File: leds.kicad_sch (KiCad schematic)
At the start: 10 parts, among them U10 SK9822, U11 SK9822, U12 SK9822, U13 SK9822, U14 SK9822

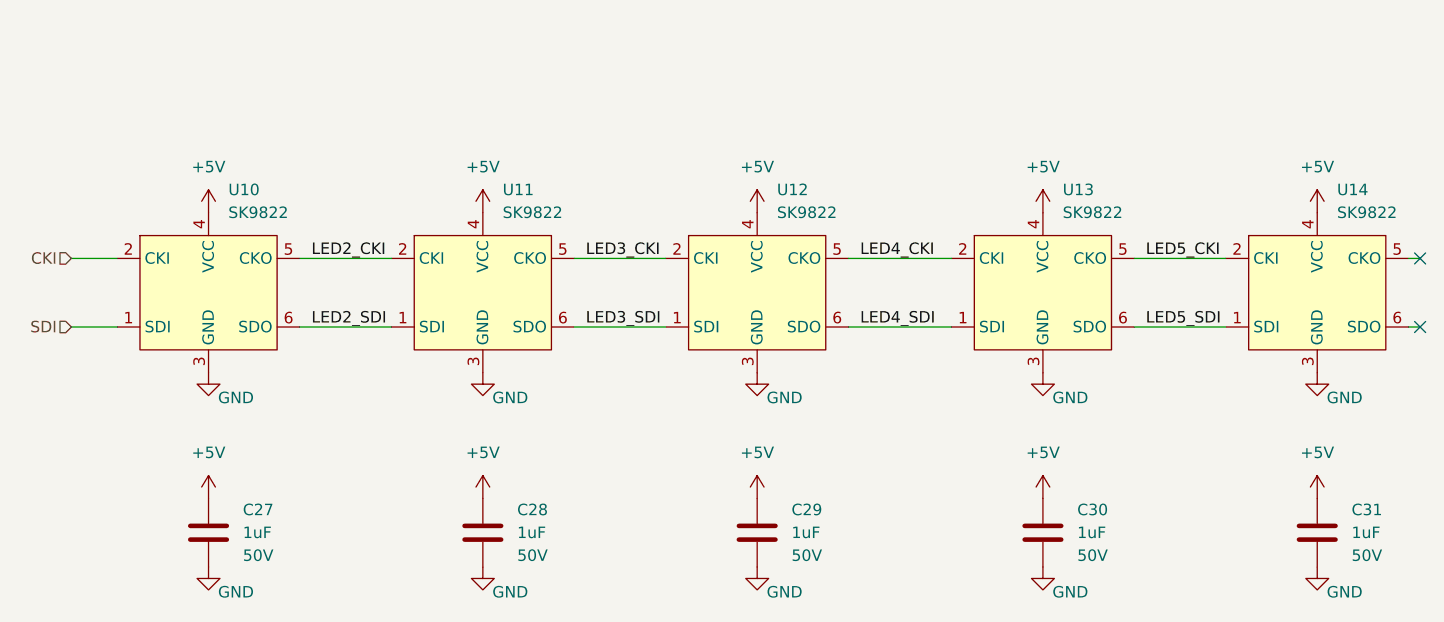
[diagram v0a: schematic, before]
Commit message: Added STM32 MCU with prelim pinout to the schematic
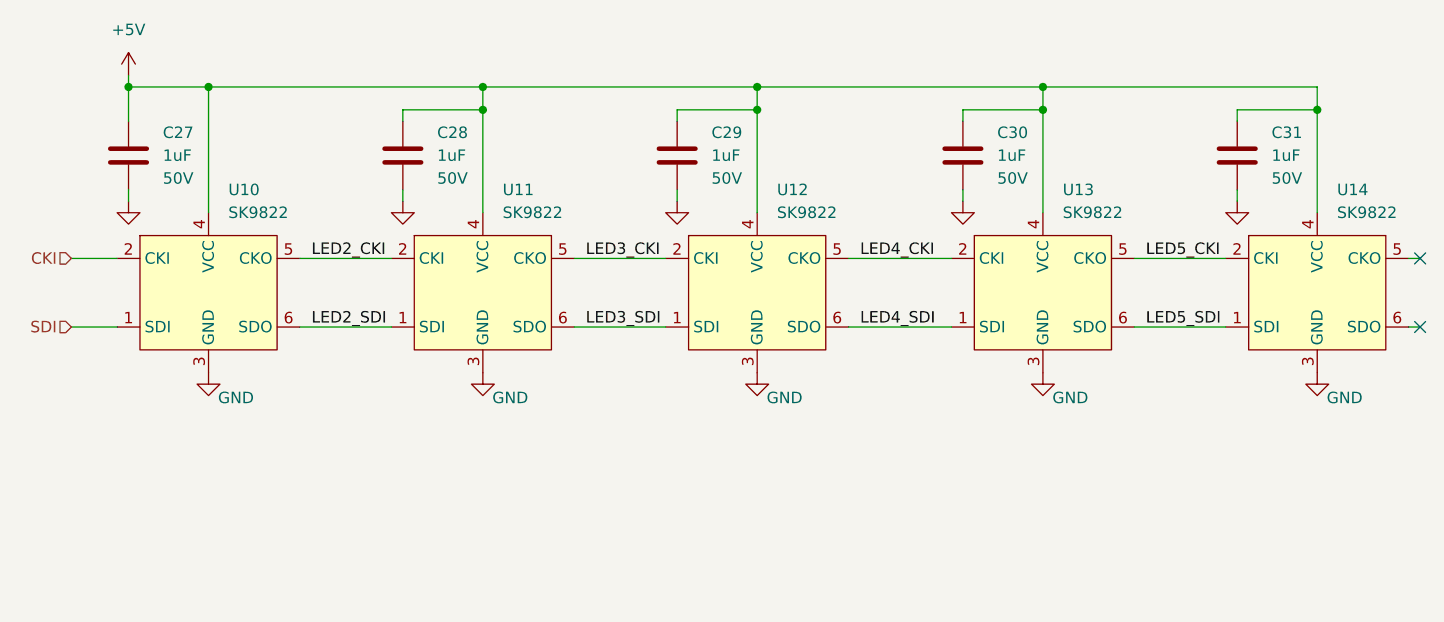
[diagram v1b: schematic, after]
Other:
- moved on the sheet: C27, C28, C29, C30, C31

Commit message: Prelim connector pinout defined.  Re-annotated all parts
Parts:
- renumbered C27 to C17, C28 to C18, C29 to C19, C30 to C20, C31 to C21, U10 to U4, U11 to U5, U12 to U6, U13 to U7, U14 to U8
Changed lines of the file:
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@@
 		(on_board yes)
 		(dnp no)
-		(property "Reference" "#PWR043"
+		(property "Reference" "#PWR0108"
 			(at 194.31 85.09 0)
 			(effects
@@
 			(project "lmc_media_blitz"
 				(path "/b87eb037-3127-4116-a225-5eb939725614/fa7871a6-f26c-496a-b2cd-c50953503e39"
-					(reference "#PWR043")
+					(reference "#PWR0108")
 					(unit 1)
 				)
@@
 		(dnp no)
 		(fields_autoplaced yes)
-		(property "Reference" "U10"
+		(property "Reference" "U4"
 			(at 82.2041 77.47 0)
 			(effects
@@
 			(project "lmc_media_blitz"
 				(path "/b87eb037-3127-4116-a225-5eb939725614/fa7871a6-f26c-496a-b2cd-c50953503e39"
-					(reference "U10")
+					(reference "U4")
 					(unit 1)
 				)
@@
 		(on_board yes)
 		(dnp no)
-		(property "Reference" "#PWR037"
+		(property "Reference" "#PWR0103"
 			(at 101.6 85.09 0)
 			(effects
@@
 			(project "lmc_media_blitz"
 				(path "/b87eb037-3127-4116-a225-5eb939725614/fa7871a6-f26c-496a-b2cd-c50953503e39"
-					(reference "#PWR037")
+					(reference "#PWR0103")
 					(unit 1)
 				)
@@
 		(on_board yes)
 		(dnp no)
-		(property "Reference" "#PWR039"
+		(property "Reference" "#PWR0102"
 			(at 132.08 85.09 0)
 			(effects
@@
 			(project "lmc_media_blitz"
 				(path "/b87eb037-3127-4116-a225-5eb939725614/fa7871a6-f26c-496a-b2cd-c50953503e39"
-					(reference "#PWR039")
+					(reference "#PWR0102")
 					(unit 1)
 				)
@@
 		(dnp no)
 		(fields_autoplaced yes)
-		(property "Reference" "U13"
+		(property "Reference" "U7"
 			(at 174.9141 77.47 0)
 			(effects
@@
 			(project "lmc_media_blitz"
 				(path "/b87eb037-3127-4116-a225-5eb939725614/fa7871a6-f26c-496a-b2cd-c50953503e39"
-					(reference "U13")
+					(reference "U7")
 					(unit 1)
 				)
@@
 		(dnp no)
 		(fields_autoplaced yes)
-		(property "Reference" "C29"
+		(property "Reference" "C19"
 			(at 135.89 71.1199 0)
 			(effects
@@
 			(project "lmc_media_blitz"
 				(path "/b87eb037-3127-4116-a225-5eb939725614/fa7871a6-f26c-496a-b2cd-c50953503e39"
-					(reference "C29")
+					(reference "C19")
 					(unit 1)
 				)
@@
 		(dnp no)
 		(fields_autoplaced yes)
-		(property "Reference" "U12"
+		(property "Reference" "U6"
 			(at 143.1641 77.47 0)
 			(effects
@@
 			(project "lmc_media_blitz"
 				(path "/b87eb037-3127-4116-a225-5eb939725614/fa7871a6-f26c-496a-b2cd-c50953503e39"
-					(reference "U12")
+					(reference "U6")
 					(unit 1)
 				)
@@
 		(on_board yes)
 		(dnp no)
-		(property "Reference" "#PWR053"
+		(property "Reference" "#PWR0105"
 			(at 80.01 104.14 0)
 			(effects
@@
 			(project "lmc_media_blitz"
 				(path "/b87eb037-3127-4116-a225-5eb939725614/fa7871a6-f26c-496a-b2cd-c50953503e39"
-					(reference "#PWR053")
+					(reference "#PWR0105")
 					(unit 1)
 				)
@@
 		(dnp no)
 		(fields_autoplaced yes)
-		(property "Reference" "U14"
+		(property "Reference" "U8"
 			(at 205.3941 77.47 0)
 			(effects
@@
 			(project "lmc_media_blitz"
 				(path "/b87eb037-3127-4116-a225-5eb939725614/fa7871a6-f26c-496a-b2cd-c50953503e39"
-					(reference "U14")
+					(reference "U8")
 					(unit 1)
 				)
@@
 		(on_board yes)
 		(dnp no)
-		(property "Reference" "#PWR034"
+		(property "Reference" "#PWR0104"
 			(at 71.12 85.09 0)
 			(effects
@@
 			(project "lmc_media_blitz"
 				(path "/b87eb037-3127-4116-a225-5eb939725614/fa7871a6-f26c-496a-b2cd-c50953503e39"
-					(reference "#PWR034")
+					(reference "#PWR0104")
 					(unit 1)
 				)
@@
 		(on_board yes)
 		(dnp no)
-		(property "Reference" "#PWR061"
+		(property "Reference" "#PWR0107"
 			(at 203.2 104.14 0)
 			(effects
@@
 			(project "lmc_media_blitz"
 				(path "/b87eb037-3127-4116-a225-5eb939725614/fa7871a6-f26c-496a-b2cd-c50953503e39"
-					(reference "#PWR061")
+					(reference "#PWR0107")
 					(unit 1)
 				)
@@
 		(dnp no)
 		(fields_autoplaced yes)
-		(property "Reference" "U11"
+		(property "Reference" "U5"
 			(at 112.6841 77.47 0)
 			(effects
@@
 			(project "lmc_media_blitz"
 				(path "/b87eb037-3127-4116-a225-5eb939725614/fa7871a6-f26c-496a-b2cd-c50953503e39"
-					(reference "U11")
+					(reference "U5")
 					(unit 1)
 				)
@@
 		(dnp no)
 		(fields_autoplaced yes)
-		(property "Reference" "#PWR052"
+		(property "Reference" "#PWR0101"
 			(at 71.12 68.58 0)
 			(effects
@@
 			(project "lmc_media_blitz"
 				(path "/b87eb037-3127-4116-a225-5eb939725614/fa7871a6-f26c-496a-b2cd-c50953503e39"
-					(reference "#PWR052")
+					(reference "#PWR0101")
 					(unit 1)
 				)
@@
 		(on_board yes)
 		(dnp no)
-		(property "Reference" "#PWR057"
+		(property "Reference" "#PWR0109"
 			(at 140.97 104.14 0)
 			(effects
@@
 			(project "lmc_media_blitz"
 				(path "/b87eb037-3127-4116-a225-5eb939725614/fa7871a6-f26c-496a-b2cd-c50953503e39"
-					(reference "#PWR057")
+					(reference "#PWR0109")
 					(unit 1)
 				)
@@
 		(dnp no)
 		(fields_autoplaced yes)
-		(property "Reference" "C27"
+		(property "Reference" "C17"
 			(at 74.93 71.1199 0)
 			(effects
@@
 			(project "lmc_media_blitz"
 				(path "/b87eb037-3127-4116-a225-5eb939725614/fa7871a6-f26c-496a-b2cd-c50953503e39"
-					(reference "C27")
+					(reference "C17")
 					(unit 1)
 				)
@@
 		(on_board yes)
 		(dnp no)
-		(property "Reference" "#PWR059"
+		(property "Reference" "#PWR0111"
 			(at 172.72 104.14 0)
 			(effects
@@
 			(project "lmc_media_blitz"
 				(path "/b87eb037-3127-4116-a225-5eb939725614/fa7871a6-f26c-496a-b2cd-c50953503e39"
-					(reference "#PWR059")
+					(reference "#PWR0111")
 					(unit 1)
 				)
@@
 		(dnp no)
 		(fields_autoplaced yes)
-		(property "Reference" "C31"
+		(property "Reference" "C21"
 			(at 198.12 71.1199 0)
 			(effects
@@
 			(project "lmc_media_blitz"
 				(path "/b87eb037-3127-4116-a225-5eb939725614/fa7871a6-f26c-496a-b2cd-c50953503e39"
-					(reference "C31")
+					(reference "C21")
 					(unit 1)
 				)
@@
 		(dnp no)
 		(fields_autoplaced yes)
-		(property "Reference" "C28"
+		(property "Reference" "C18"
 			(at 105.41 71.1199 0)
 			(effects
@@
 			(project "lmc_media_blitz"
 				(path "/b87eb037-3127-4116-a225-5eb939725614/fa7871a6-f26c-496a-b2cd-c50953503e39"
-					(reference "C28")
+					(reference "C18")
 					(unit 1)
 				)
@@
 		(on_board yes)
 		(dnp no)
-		(property "Reference" "#PWR055"
+		(property "Reference" "#PWR0106"
 			(at 110.49 104.14 0)
 			(effects
@@
 			(project "lmc_media_blitz"
 				(path "/b87eb037-3127-4116-a225-5eb939725614/fa7871a6-f26c-496a-b2cd-c50953503e39"
-					(reference "#PWR055")
+					(reference "#PWR0106")
 					(unit 1)
 				)
@@
 		(dnp no)
 		(fields_autoplaced yes)
-		(property "Reference" "C30"
+		(property "Reference" "C20"
 			(at 167.64 71.1199 0)
 			(effects
@@
 			(project "lmc_media_blitz"
 				(path "/b87eb037-3127-4116-a225-5eb939725614/fa7871a6-f26c-496a-b2cd-c50953503e39"
-					(reference "C30")
+					(reference "C20")
 					(unit 1)
 				)
@@
 		(on_board yes)
 		(dnp no)
-		(property "Reference" "#PWR041"
+		(property "Reference" "#PWR0110"
 			(at 163.83 85.09 0)
 			(effects
@@
 			(project "lmc_media_blitz"
 				(path "/b87eb037-3127-4116-a225-5eb939725614/fa7871a6-f26c-496a-b2cd-c50953503e39"
-					(reference "#PWR041")
-					(unit 1)
-				)
+					(reference "#PWR0110")
+					(unit 1)
+				)

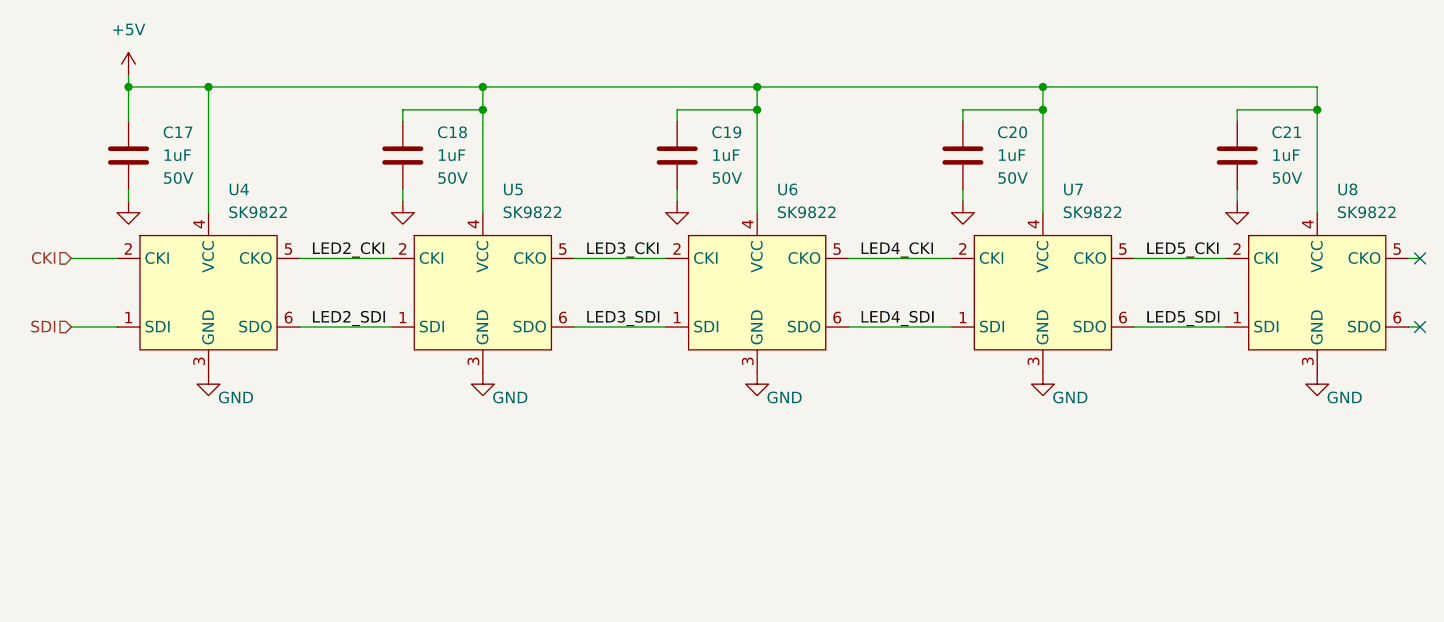
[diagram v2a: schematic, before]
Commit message: Added I2C resistors to schematic, cleaned up unused parts and started layout
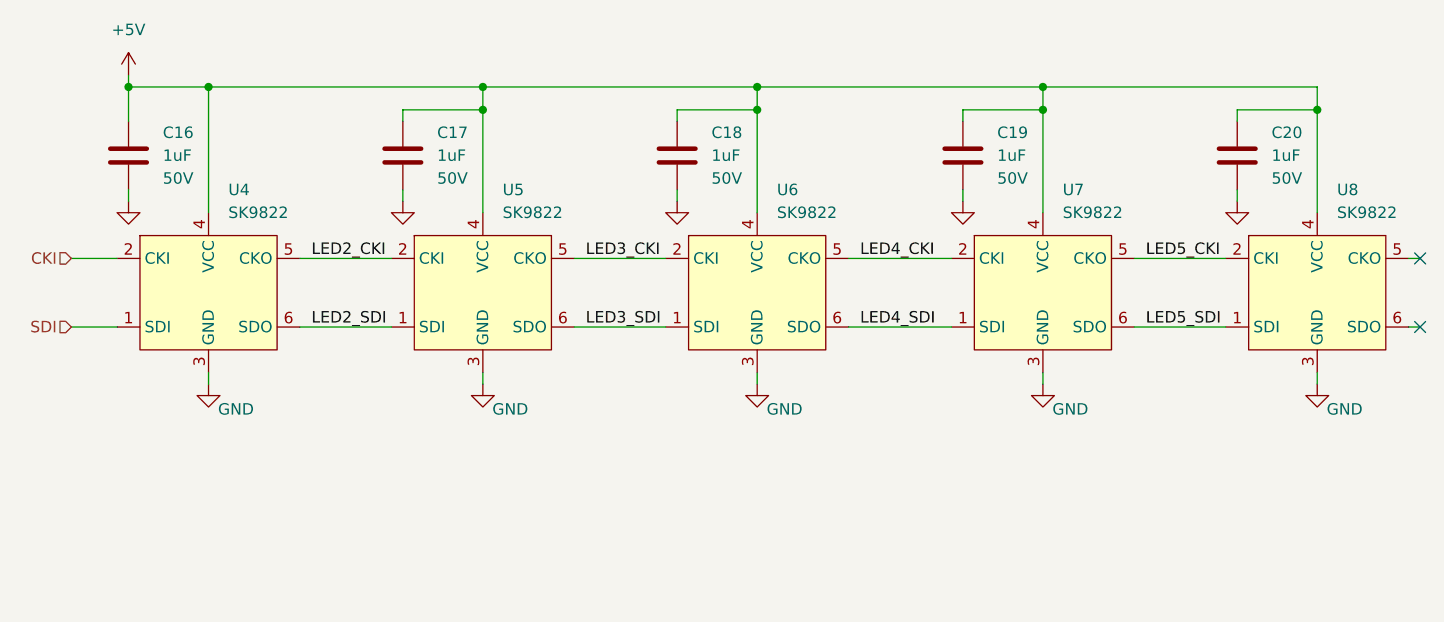
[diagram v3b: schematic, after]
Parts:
- renumbered C17 to C16, C18 to C17, C19 to C18, C20 to C19, C21 to C20
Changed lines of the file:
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@@
+	(wire
+		(pts
+			(xy 110.49 99.06) (xy 110.49 97.79)
+		)
+		(stroke
+			(width 0)
+			(type default)
+		)
+	)
 	(wire
 		(pts
@@
 	(wire
 		(pts
+			(xy 80.01 99.06) (xy 80.01 97.79)
+		)
+		(stroke
+			(width 0)
+			(type default)
+		)
+	)
+	(wire
+		(pts
 			(xy 120.65 85.09) (xy 130.81 85.09)
 		)
@@
 	(wire
 		(pts
+			(xy 140.97 99.06) (xy 140.97 97.79)
+		)
+		(stroke
+			(width 0)
+			(type default)
+		)
+	)
+	(wire
+		(pts
 			(xy 163.83 68.58) (xy 172.72 68.58)
 		)
@@
 		(pts
 			(xy 80.01 66.04) (xy 80.01 80.01)
+		)
+		(stroke
+			(width 0)
+			(type default)
+		)
+	)
+	(wire
+		(pts
+			(xy 172.72 99.06) (xy 172.72 97.79)
+		)
+		(stroke
+			(width 0)
+			(type default)
+		)
+	)
+	(wire
+		(pts
+			(xy 203.2 99.06) (xy 203.2 97.79)
 		)
 		(stroke
@@
 		(dnp no)
 		(fields_autoplaced yes)
-		(property "Reference" "C19"
+		(property "Reference" "C18"
 			(at 135.89 71.1199 0)
 			(effects
@@
 			(project "lmc_media_blitz"
 				(path "/b87eb037-3127-4116-a225-5eb939725614/fa7871a6-f26c-496a-b2cd-c50953503e39"
-					(reference "C19")
+					(reference "C18")
 					(unit 1)
 				)
@@
 	(symbol
 		(lib_id "power:GND")
-		(at 80.01 97.79 0)
+		(at 80.01 99.06 0)
 		(unit 1)
 		(exclude_from_sim no)
@@
 		(dnp no)
 		(property "Reference" "#PWR0105"
-			(at 80.01 104.14 0)
+			(at 80.01 105.41 0)
 			(effects
 				(font
@@
 		)
 		(property "Value" "GND"
-			(at 83.058 100.584 0)
+			(at 83.058 101.854 0)
 			(effects
 				(font
@@
 		)
 		(property "Footprint" ""
-			(at 80.01 97.79 0)
+			(at 80.01 99.06 0)
 			(effects
 				(font
@@
 		)
 		(property "Datasheet" ""
-			(at 80.01 97.79 0)
+			(at 80.01 99.06 0)
 			(effects
 				(font
@@
 		)
 		(property "Description" "Power symbol creates a global label with name \"GND\" , ground"
-			(at 80.01 97.79 0)
+			(at 80.01 99.06 0)
 			(effects
 				(font
@@
 	(symbol
 		(lib_id "power:GND")
-		(at 203.2 97.79 0)
+		(at 203.2 99.06 0)
 		(unit 1)
 		(exclude_from_sim no)
@@
 		(dnp no)
 		(property "Reference" "#PWR0107"
-			(at 203.2 104.14 0)
+			(at 203.2 105.41 0)
 			(effects
 				(font
@@
 		)
 		(property "Value" "GND"
-			(at 206.248 100.584 0)
+			(at 206.248 101.854 0)
 			(effects
 				(font
@@
 		)
 		(property "Footprint" ""
-			(at 203.2 97.79 0)
+			(at 203.2 99.06 0)
 			(effects
 				(font
@@
 		)
 		(property "Datasheet" ""
-			(at 203.2 97.79 0)
+			(at 203.2 99.06 0)
 			(effects
 				(font
@@
 		)
 		(property "Description" "Power symbol creates a global label with name \"GND\" , ground"
-			(at 203.2 97.79 0)
+			(at 203.2 99.06 0)
 			(effects
 				(font
@@
 	(symbol
 		(lib_id "power:GND")
-		(at 140.97 97.79 0)
+		(at 140.97 99.06 0)
 		(unit 1)
 		(exclude_from_sim no)
@@
 		(dnp no)
 		(property "Reference" "#PWR0109"
-			(at 140.97 104.14 0)
+			(at 140.97 105.41 0)
 			(effects
 				(font
@@
 		)
 		(property "Value" "GND"
-			(at 144.018 100.584 0)
+			(at 144.018 101.854 0)
 			(effects
 				(font
@@
 		)
 		(property "Footprint" ""
-			(at 140.97 97.79 0)
+			(at 140.97 99.06 0)
 			(effects
 				(font
@@
 		)
 		(property "Datasheet" ""
-			(at 140.97 97.79 0)
+			(at 140.97 99.06 0)
 			(effects
 				(font
@@
 		)
 		(property "Description" "Power symbol creates a global label with name \"GND\" , ground"
-			(at 140.97 97.79 0)
+			(at 140.97 99.06 0)
 			(effects
 				(font
@@
 		(dnp no)
 		(fields_autoplaced yes)
-		(property "Reference" "C17"
+		(property "Reference" "C16"
 			(at 74.93 71.1199 0)
 			(effects
@@
 			(project "lmc_media_blitz"
 				(path "/b87eb037-3127-4116-a225-5eb939725614/fa7871a6-f26c-496a-b2cd-c50953503e39"
-					(reference "C17")
+					(reference "C16")
 					(unit 1)
 				)
@@
 	(symbol
 		(lib_id "power:GND")
-		(at 172.72 97.79 0)
+		(at 172.72 99.06 0)
 		(unit 1)
 		(exclude_from_sim no)
@@
 		(dnp no)
 		(property "Reference" "#PWR0111"
-			(at 172.72 104.14 0)
+			(at 172.72 105.41 0)
 			(effects
 				(font
@@
 		)
 		(property "Value" "GND"
-			(at 175.768 100.584 0)
+			(at 175.768 101.854 0)
 			(effects
 				(font
@@
 		)
 		(property "Footprint" ""
-			(at 172.72 97.79 0)
+			(at 172.72 99.06 0)
 			(effects
 				(font
@@
 		)
 		(property "Datasheet" ""
-			(at 172.72 97.79 0)
+			(at 172.72 99.06 0)
 			(effects
 				(font
@@
 		)
 		(property "Description" "Power symbol creates a global label with name \"GND\" , ground"
-			(at 172.72 97.79 0)
+			(at 172.72 99.06 0)
 			(effects
 				(font
@@
 		(dnp no)
 		(fields_autoplaced yes)
-		(property "Reference" "C21"
+		(property "Reference" "C20"
 			(at 198.12 71.1199 0)
 			(effects
@@
 			(project "lmc_media_blitz"
 				(path "/b87eb037-3127-4116-a225-5eb939725614/fa7871a6-f26c-496a-b2cd-c50953503e39"
-					(reference "C21")
+					(reference "C20")
 					(unit 1)
 				)
@@
 		(dnp no)
 		(fields_autoplaced yes)
-		(property "Reference" "C18"
+		(property "Reference" "C17"
 			(at 105.41 71.1199 0)
 			(effects
@@
 			(project "lmc_media_blitz"
 				(path "/b87eb037-3127-4116-a225-5eb939725614/fa7871a6-f26c-496a-b2cd-c50953503e39"
-					(reference "C18")
+					(reference "C17")
 					(unit 1)
 				)
@@
 	(symbol
 		(lib_id "power:GND")
-		(at 110.49 97.79 0)
+		(at 110.49 99.06 0)
 		(unit 1)
 		(exclude_from_sim no)
@@
 		(dnp no)
 		(property "Reference" "#PWR0106"
-			(at 110.49 104.14 0)
+			(at 110.49 105.41 0)
 			(effects
 				(font
@@
 		)
 		(property "Value" "GND"
-			(at 113.538 100.584 0)
+			(at 113.538 101.854 0)
 			(effects
 				(font
@@
 		)
 		(property "Footprint" ""
-			(at 110.49 97.79 0)
+			(at 110.49 99.06 0)
 			(effects
 				(font
@@
 		)
 		(property "Datasheet" ""
-			(at 110.49 97.79 0)
+			(at 110.49 99.06 0)
 			(effects
 				(font
@@
 		)
 		(property "Description" "Power symbol creates a global label with name \"GND\" , ground"
-			(at 110.49 97.79 0)
+			(at 110.49 99.06 0)
 			(effects
 				(font
@@
 		(dnp no)
 		(fields_autoplaced yes)
-		(property "Reference" "C20"
+		(property "Reference" "C19"
 			(at 167.64 71.1199 0)
 			(effects
@@
 			(project "lmc_media_blitz"
 				(path "/b87eb037-3127-4116-a225-5eb939725614/fa7871a6-f26c-496a-b2cd-c50953503e39"
-					(reference "C20")
+					(reference "C19")
 					(unit 1)
 				)
